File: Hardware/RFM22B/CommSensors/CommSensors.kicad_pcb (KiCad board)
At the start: 2 copper layers, 57.3 x 54.2 mm, 4 parts

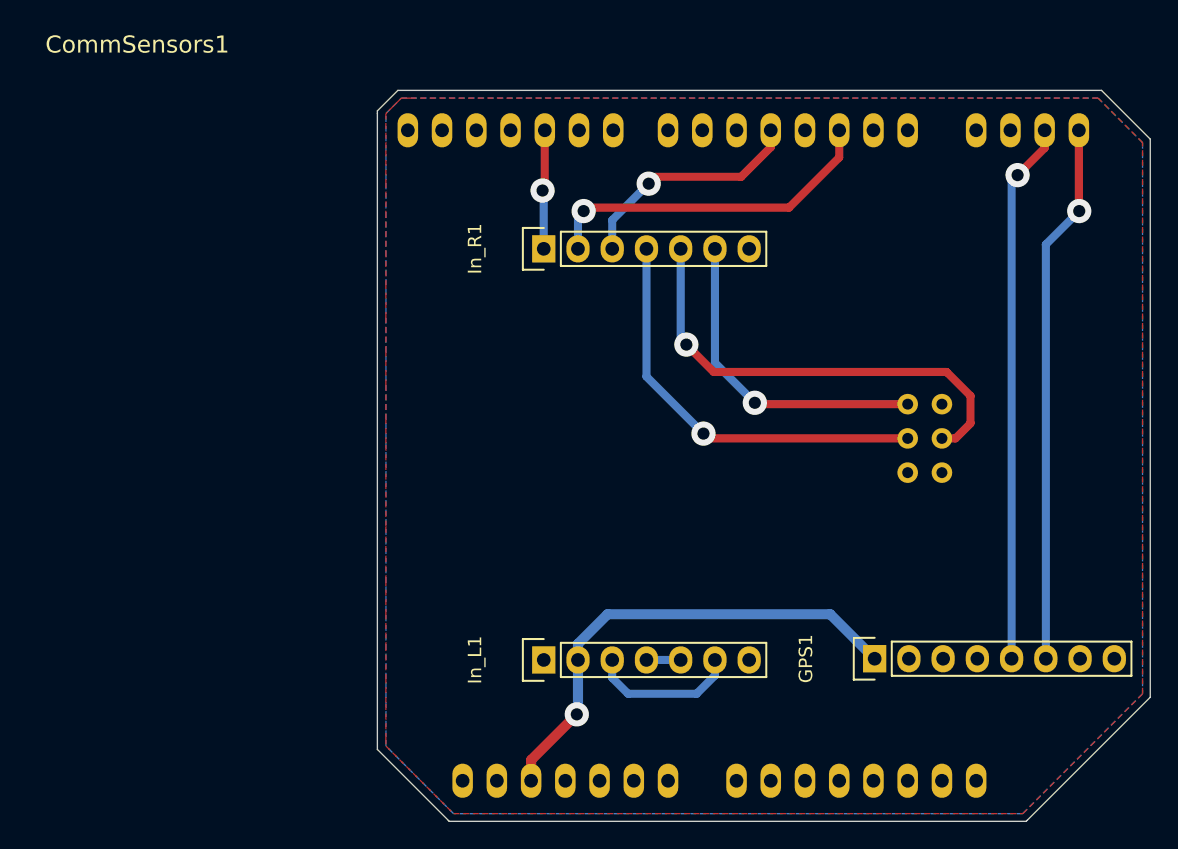
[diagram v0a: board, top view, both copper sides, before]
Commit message: Added Doc file with the datasheets of the hardware used. \nChanged the modulation for the GPS test (GFSK to FSK). \nDeleted unnecesary variables from TX_GPS.ino.
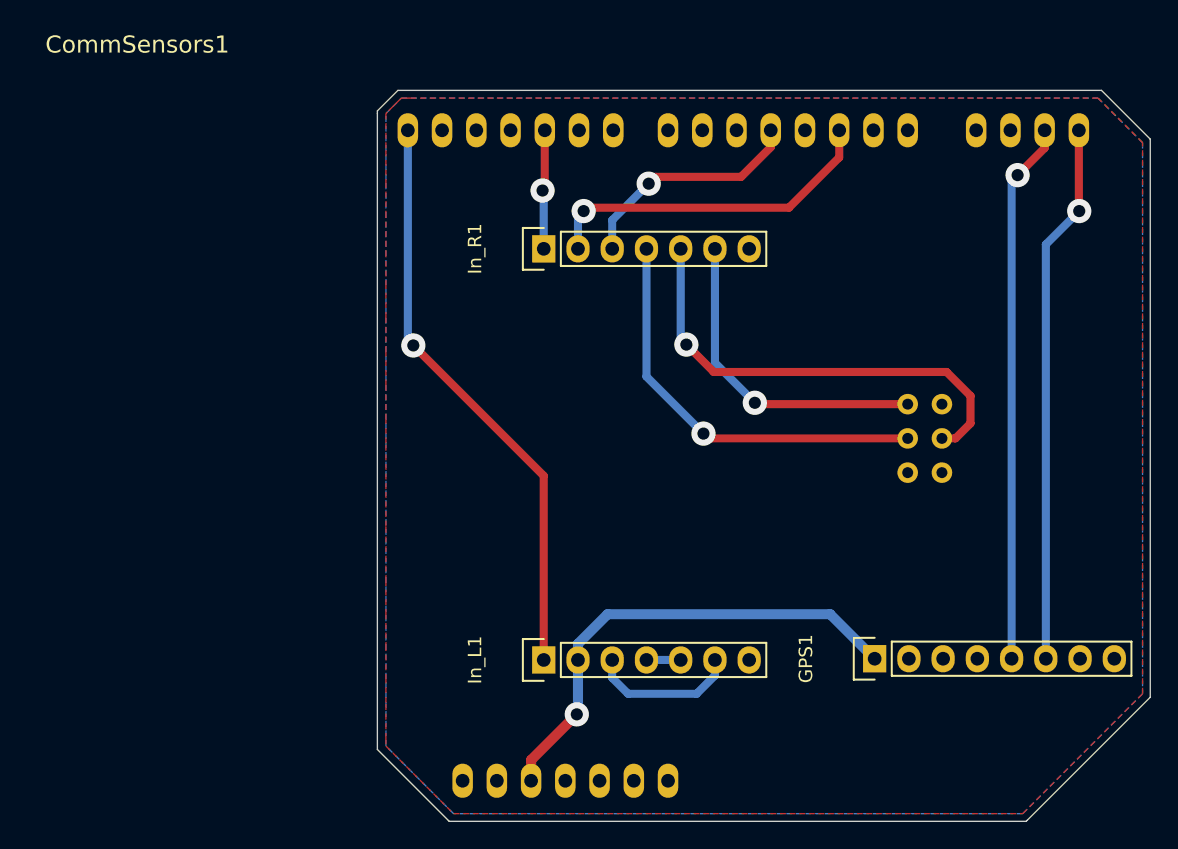
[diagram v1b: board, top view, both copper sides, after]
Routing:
- net GND: track 0.00 -> 43.5 mm, vias 0 -> 1
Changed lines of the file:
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@@
     (thickness 1.6)
     (drawings 11)
-    (tracks 64)
+    (tracks 69)
     (zones 0)
     (modules 4)
@@
     (pad 17 thru_hole oval (at 76.2 -50.8 90) (size 2.54 1.524) (drill 1.016) (layers *.Cu *.Mask F.SilkS)
       (net 2 /TX))
-    (pad AD7 thru_hole oval (at 68.58 -2.54 90) (size 2.54 1.524) (drill 1.016) (layers *.Cu *.Mask F.SilkS))
-    (pad AD6 thru_hole oval (at 66.04 -2.54 90) (size 2.54 1.524) (drill 1.016) (layers *.Cu *.Mask F.SilkS))
-    (pad AD5 thru_hole oval (at 63.5 -2.54 90) (size 2.54 1.524) (drill 1.016) (layers *.Cu *.Mask F.SilkS))
-    (pad AD4 thru_hole oval (at 60.96 -2.54 90) (size 2.54 1.524) (drill 1.016) (layers *.Cu *.Mask F.SilkS))
-    (pad AD3 thru_hole oval (at 58.42 -2.54 90) (size 2.54 1.524) (drill 1.016) (layers *.Cu *.Mask F.SilkS))
-    (pad AD0 thru_hole oval (at 50.8 -2.54 90) (size 2.54 1.524) (drill 1.016) (layers *.Cu *.Mask F.SilkS))
-    (pad AD1 thru_hole oval (at 53.34 -2.54 90) (size 2.54 1.524) (drill 1.016) (layers *.Cu *.Mask F.SilkS))
-    (pad AD2 thru_hole oval (at 55.88 -2.54 90) (size 2.54 1.524) (drill 1.016) (layers *.Cu *.Mask F.SilkS))
     (pad V_IN thru_hole oval (at 45.72 -2.54 90) (size 2.54 1.524) (drill 1.016) (layers *.Cu *.Mask F.SilkS))
     (pad GND2 thru_hole oval (at 43.18 -2.54 90) (size 2.54 1.524) (drill 1.016) (layers *.Cu *.Mask F.SilkS)
@@
   (via (at 224.7265 60.198) (size 1.8) (drill 0.9) (layers F.Cu B.Cu) (net 2))
   (segment (start 222.25 62.6745) (end 224.7265 60.198) (width 0.6) (layer B.Cu) (net 2))
+  (segment (start 185 93.5) (end 185 79.844) (width 0.6) (layer F.Cu) (net 3))
+  (segment (start 174.9171 69.7611) (end 174.9171 54.2036) (width 0.6) (layer B.Cu) (net 3))
+  (segment (start 175.3235 70.1675) (end 174.9171 69.7611) (width 0.6) (layer B.Cu) (net 3))
+  (via (at 175.3235 70.1675) (size 1.8) (drill 0.9) (layers F.Cu B.Cu) (net 3))
+  (segment (start 185 79.844) (end 175.3235 70.1675) (width 0.6) (layer F.Cu) (net 3))
   (segment (start 187.54 93.5) (end 187.54 92.3045) (width 0.75) (layer B.Cu) (net 4))
   (segment (start 206.248 90.1065) (end 209.55 93.4085) (width 0.75) (layer B.Cu) (net 4))
